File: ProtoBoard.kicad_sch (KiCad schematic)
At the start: 51 parts, among them J1 Conn_01x03_Female, J2 TYPE-C-31-M-12, J3 Conn_01x04_Female, J4 Conn_01x10_Female, J5 Conn_01x05_Female, J6 Conn_01x05_Female, J7 Conn_01x10_Female, J8 Conn_01x05_Female, J9 Conn_01x10_Female, Q1 HX2300A, Q2 HX2300A, SW1 SW_Push, SW2 SW_Push, U1 ESP32-S3-MINI-1, U2 CD74HC4067SM, U3 LM1084-5.0, U4 HY2120, U5 WS2812-2020, U6 LM1084-3.3

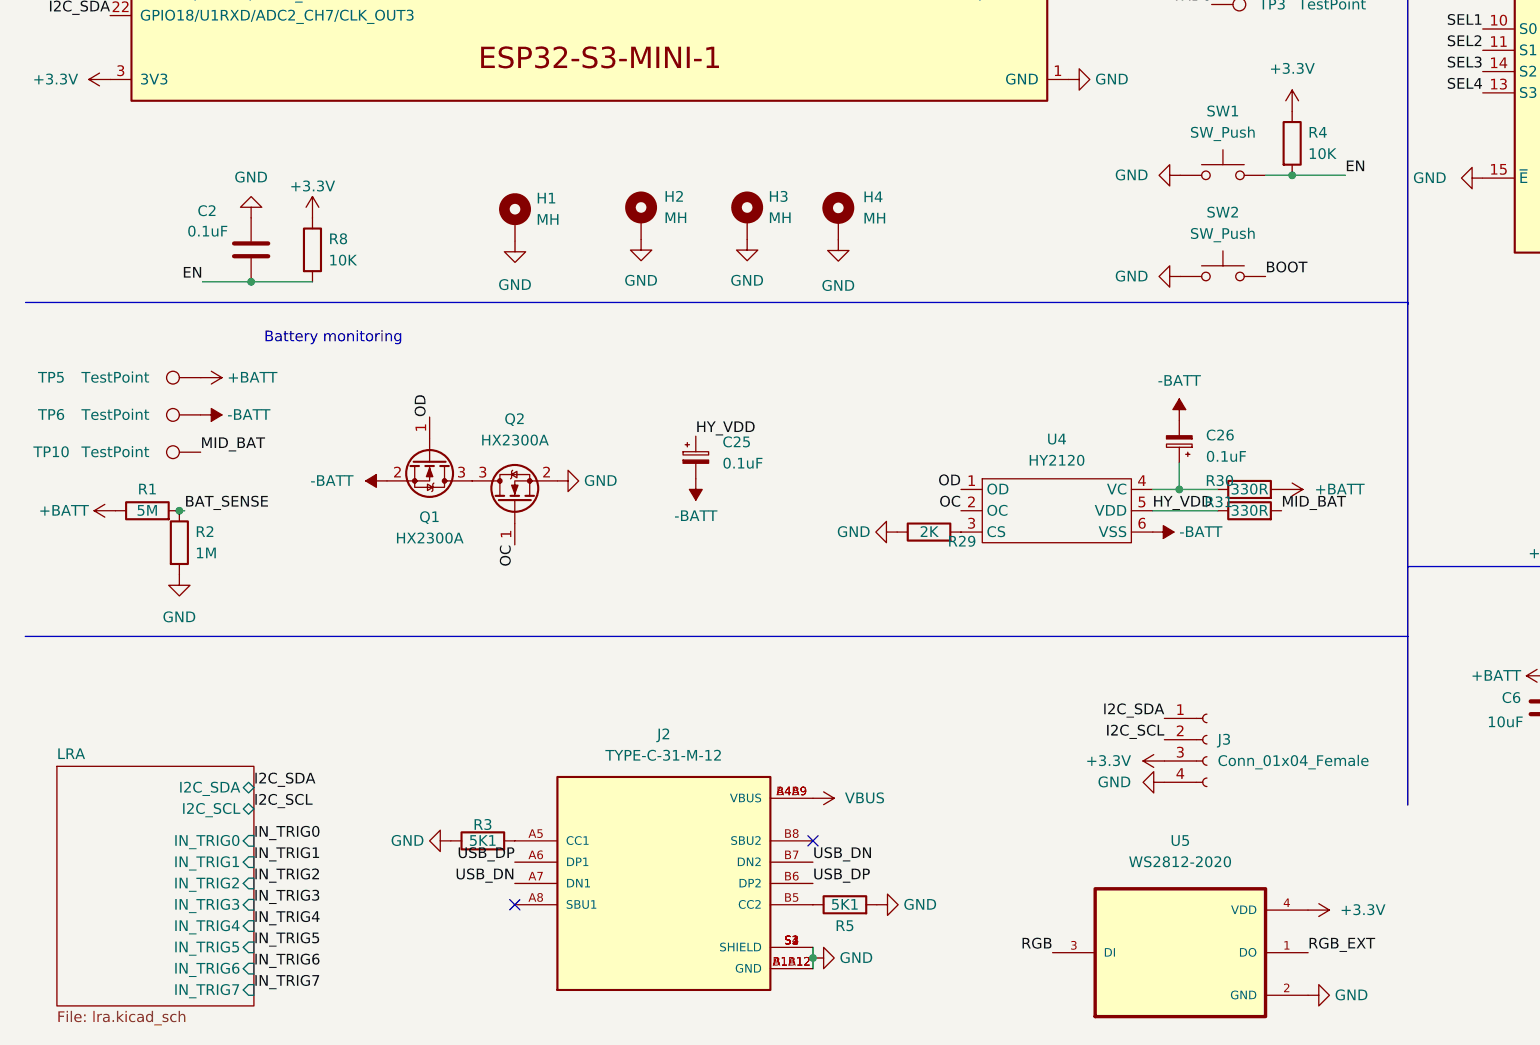
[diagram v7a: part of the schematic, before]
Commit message: Fix bms + a bit clearer schematic
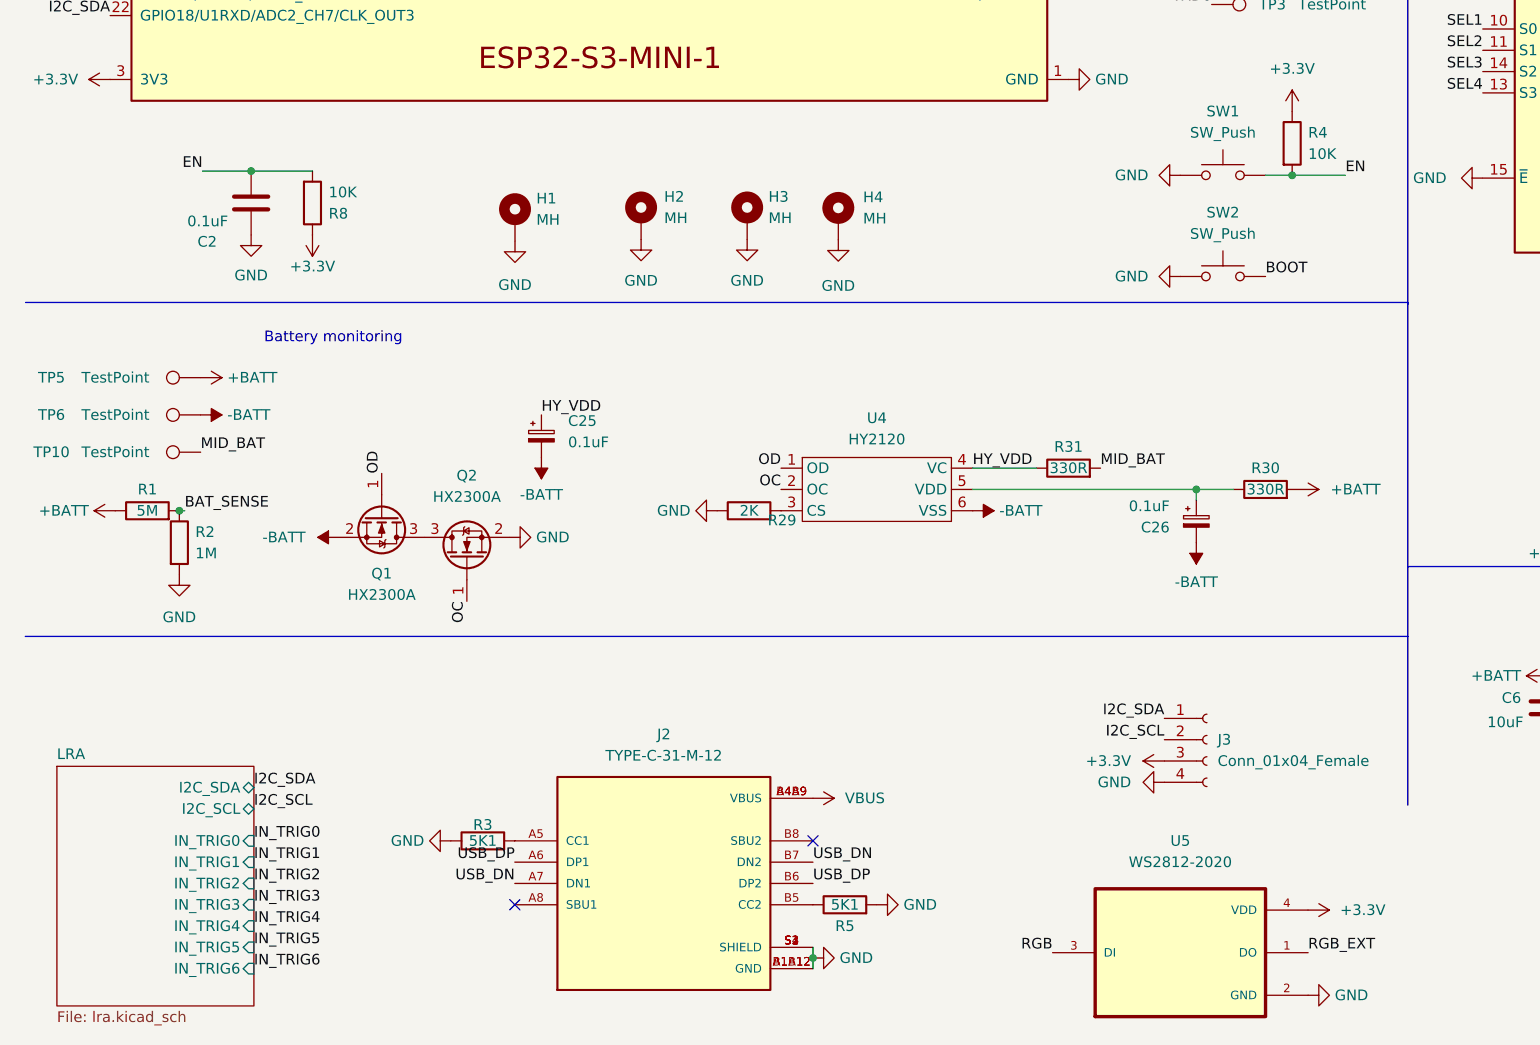
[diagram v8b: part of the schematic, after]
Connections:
- net HY_VDD: now also U4.4 (VC); no longer U4.5 (VDD)
- net at C26.1, R30.1: now also U4.5 (VDD); no longer U4.4 (VC)
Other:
- sheet LRA ports: added none; removed IN_TRIG7
- moved on the sheet: C2, C25, C26, Q1, Q2, R29, R30, R31, R8, U4
